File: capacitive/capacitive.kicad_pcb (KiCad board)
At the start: 2 copper layers, 54 parts, among them J102 UART, J103 SWD, J104 TX_PADS, J105 RX_PAD, J106 POWER, Q101 RU1C002ZPTCL, SW101 SW_Push, U101 STM32F070C6T6, U102 TLV9062IDR, U103 SG7050CAN_8.000000M-TJGA3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

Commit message: Generate first revision Gerber files
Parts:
- removed U105: D3V3X4U10LP-7, capacitive:Diode_U-DFN2510-10
- added C107: 100nF 20%, Capacitors_SMD:C_0805_HandSoldering, F.Cu at (113.9, 107.3)
- added D101: ESD9B3.3ST5G, capacitive:SOD-923, F.Cu at (120.3, 75.4)
- added D103: ESD9B3.3ST5G, capacitive:SOD-923, F.Cu at (120.3, 72.5)
- added J101: UL, capacitive:Slide_Drill_Left, F.Cu at (100.0, 95.0)
- added J107: UR, capacitive:Slide_Drill_Right, F.Cu at (100.0, 85.0)
- added J108: LL, capacitive:Slide_Drill_Left, F.Cu at (100.0, 114.0)
- added J109: LR, capacitive:Slide_Drill_Right, F.Cu at (100.0, 115.0)
- added R107: 100k 1%, Resistors_SMD:R_1206_HandSoldering, F.Cu at (113.1, 93.2)
- added R112: 100k 1%, Resistors_SMD:R_1206_HandSoldering, F.Cu at (115.8, 93.1)
- RV102: value 100k linear -> 5k linear; footprint capacitive:Vishay_T73YE -> capacitive:Bourns-PVG5H
- moved TP107 192.4 mm to (87.7, 84.6)
- moved TP109 181.0 mm to (91.3, 67.2)
- moved TP101 150.6 mm to (83.2, 66.4)
- moved TP108 137.2 mm to (125.9, 112.7)
- moved TP102 117.1 mm to (122.2, 112.8), turned to 180 degrees
- moved R101 37.6 mm to (124.4, 106.3), turned to 0 degrees
- moved R105 34.3 mm to (116.0, 109.6), turned to 180 degrees
- moved C118 34.2 mm to (95.6, 58.3)
- moved C110 32.0 mm to (119.4, 106.4), turned to 180 degrees
- moved R106 31.2 mm to (113.9, 105.5), turned to 0 degrees
- moved C113 31.1 mm to (72.3, 88.1), turned to 180 degrees
- moved C103 29.9 mm to (125.2, 100.7), turned to 90 degrees
- moved TP106 28.8 mm to (108.5, 98.8)
- moved R102 28.3 mm to (122.9, 109.6), turned to 180 degrees
- moved U102 27.9 mm to (120.8, 100.7), turned to 180 degrees
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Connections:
- RV101 pad 1: Net-(R101-Pad2) -> Net-(R103-Pad1)
- RV101 pad 3: Net-(R103-Pad1) -> Net-(R101-Pad2)
- RV102 pad 1: GND -> Net-(R107-Pad2)
- RV102 pad 3: +3.3VA -> Net-(R112-Pad1)
- U101 pad 16: /PHASE4 -> /PHASE0
- U101 pad 17: /PHASE5 -> /PHASE2
- U101 pad 18: /PHASE6 -> /PHASE4
- U101 pad 19: /PHASE7 -> /PHASE6
- U101 pad 29: /PHASE0 -> /PHASE1
- U101 pad 30: /PHASE1 -> /PHASE3
- U101 pad 31: /PHASE2 -> /PHASE5
- U101 pad 32: /PHASE3 -> /PHASE7
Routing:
- net GND: track 0.00 -> 440.9 mm, vias 0 -> 27
- net +3V3: track 0.00 -> 145.7 mm, vias 0 -> 2
- net +3.3VA: track 0.00 -> 133.0 mm, vias 0 -> 5
- net /RX_PAD: track 0.00 -> 78.6 mm, vias 0 -> 4
- net +5V: track 0.00 -> 50.1 mm, vias 0 -> 3
- net /PHASE5: track 0.00 -> 45.8 mm, vias 0 -> 6
- net /PHASE0: track 0.00 -> 45.4 mm, vias 0 -> 6
- net /PHASE7: track 0.00 -> 45.0 mm, vias 0 -> 6
- net /PHASE2: track 0.00 -> 44.3 mm, vias 0 -> 6
- net /PHASE4: track 0.00 -> 43.8 mm, vias 0 -> 6
- net /PHASE6: track 0.00 -> 43.8 mm, vias 0 -> 6
- net /PHASE3: track 0.00 -> 43.3 mm, vias 0 -> 6
- net /PHASE1: track 0.00 -> 43.1 mm, vias 0 -> 6
- net /UART_RX: track 0.00 -> 40.7 mm, vias 0 -> 2
- net /UART_TX: track 0.00 -> 38.5 mm, vias 0 -> 2
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- added copper zone on F.Cu, net /RX_PAD
- added copper zone on B.Cu, net GND
- added copper zone on F.Cu, net GND
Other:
- board outline added: 61 x 77 mm

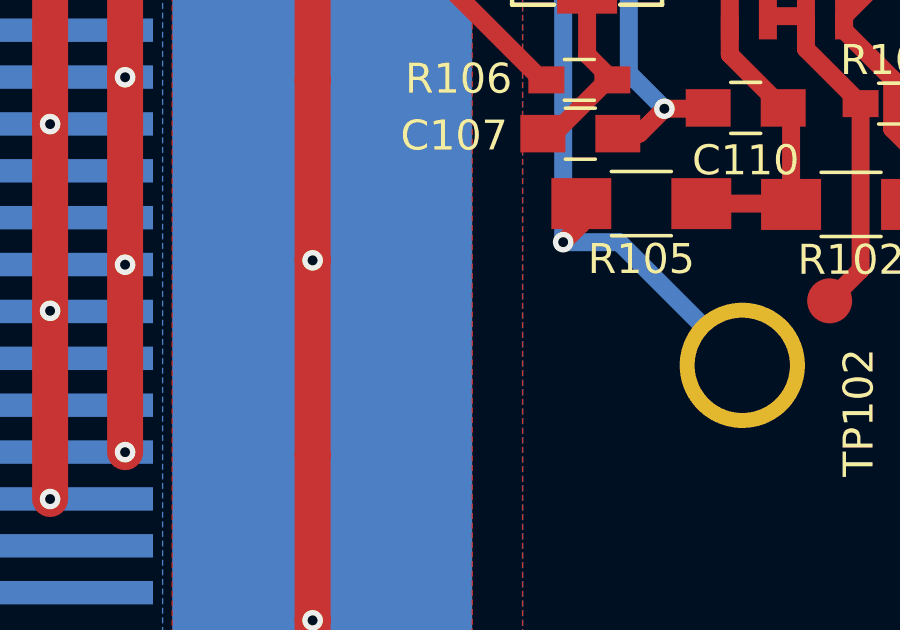
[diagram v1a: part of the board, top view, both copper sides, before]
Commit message: Add input capacitor to help set the input roll-off frequency; it seems to reduce ripple a fair amount
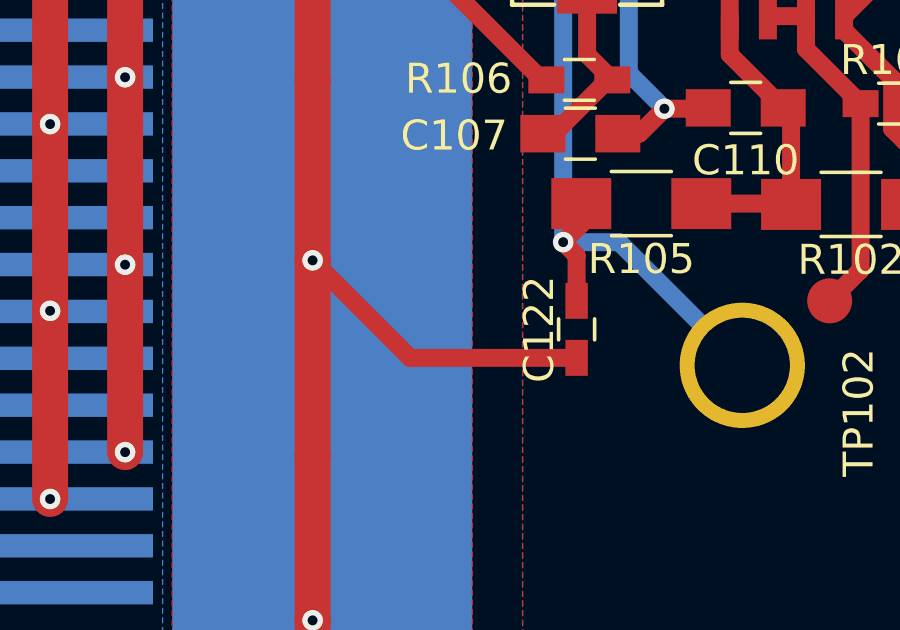
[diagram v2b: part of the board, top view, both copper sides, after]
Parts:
- added C122: 16pF 5%, Capacitors_SMD:C_0603_HandSoldering, F.Cu at (113.8, 113.8)
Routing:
- net /RX_PAD: track 78.6 -> 88.8 mm
- net GND: track 440.9 -> 443.1 mm
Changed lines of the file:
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@@
 (kicad_pcb (version 4) (host pcbnew 4.0.7)
   (general
-    (links 169)
+    (links 171)
     (no_connects 0)
     (area 66.924999 51.924999 128.075001 129.075001)
     (thickness 1.6)
     (drawings 4)
-    (tracks 721)
+    (tracks 725)
     (zones 0)
-    (modules 62)
+    (modules 63)
     (nets 33)
   )
@@
   )
   (setup
-    (last_trace_width 0.3)
+    (last_trace_width 0.6)
     (user_trace_width 0.3)
     (user_trace_width 0.45)
@@
     )
   )
+  (module Capacitors_SMD:C_0603_HandSoldering (layer F.Cu)
+    (at 113.8 113.8 90)
+    (descr "Capacitor SMD 0603, hand soldering")
+    (tags "capacitor 0603")
+    (attr smd)
+    (fp_text reference C122 (at 0 -1.25 90) (layer F.SilkS)
+      (effects (font (size 1 1) (thickness 0.15)))
+    )
+    (fp_text value "16pF 5%" (at 0 1.5 90) (layer F.Fab)
+      (effects (font (size 1 1) (thickness 0.15)))
+    )
+    (fp_text user %R (at 0 -1.25 90) (layer F.Fab)
+      (effects (font (size 1 1) (thickness 0.15)))
+    )
+    (fp_line (start -0.8 0.4) (end -0.8 -0.4) (layer F.Fab) (width 0.1))
+    (fp_line (start 0.8 0.4) (end -0.8 0.4) (layer F.Fab) (width 0.1))
+    (fp_line (start 0.8 -0.4) (end 0.8 0.4) (layer F.Fab) (width 0.1))
+    (fp_line (start -0.8 -0.4) (end 0.8 -0.4) (layer F.Fab) (width 0.1))
+    (fp_line (start -0.35 -0.6) (end 0.35 -0.6) (layer F.SilkS) (width 0.12))
+    (fp_line (start 0.35 0.6) (end -0.35 0.6) (layer F.SilkS) (width 0.12))
+    (fp_line (start -1.8 -0.65) (end 1.8 -0.65) (layer F.CrtYd) (width 0.05))
+    (fp_line (start -1.8 -0.65) (end -1.8 0.65) (layer F.CrtYd) (width 0.05))
+    (fp_line (start 1.8 0.65) (end 1.8 -0.65) (layer F.CrtYd) (width 0.05))
+    (fp_line (start 1.8 0.65) (end -1.8 0.65) (layer F.CrtYd) (width 0.05))
+    (pad 1 smd rect (at -0.95 0 90) (size 1.2 0.75) (layers F.Cu F.Paste F.Mask)
+      (net 23 /RX_PAD))
+    (pad 2 smd rect (at 0.95 0 90) (size 1.2 0.75) (layers F.Cu F.Paste F.Mask)
+      (net 2 GND))
+    (model Capacitors_SMD.3dshapes/C_0603.wrl
+      (at (xyz 0 0 0))
+      (scale (xyz 1 1 1))
+      (rotate (xyz 0 0 0))
+    )
+  )
   (gr_line (start 67 129) (end 67 52) (layer Edge.Cuts) (width 0.15))
   (gr_line (start 128 129) (end 67 129) (layer Edge.Cuts) (width 0.15))
@@
   (segment (start 75.806526 67.71386) (end 76.770596 67.71386) (width 1.2) (layer F.Cu) (net 1))
   (segment (start 76.770596 67.71386) (end 77.75448 67.71386) (width 1.2) (layer F.Cu) (net 1))
+  (segment (start 113.8 112.85) (end 113.8 111.34128) (width 0.6) (layer F.Cu) (net 2))
+  (segment (start 113.8 111.34128) (end 113.35258 110.89386) (width 0.6) (layer F.Cu) (net 2))
   (segment (start 87.03564 77.29728) (end 89.93124 80.19288) (width 0.3) (layer B.Cu) (net 2))
   (segment (start 89.93124 80.19288) (end 91.46794 80.19288) (width 0.3) (layer B.Cu) (net 2))
@@
   (via (at 98.75 111.6457) (size 0.6858) (drill 0.3302) (layers F.Cu B.Cu) (net 22))
   (via (at 98.75 117.8941) (size 0.6858) (drill 0.3302) (layers F.Cu B.Cu) (net 22))
+  (segment (start 113.8 114.75) (end 108.25 114.75) (width 0.6) (layer F.Cu) (net 23))
+  (segment (start 108.25 114.75) (end 105 111.5) (width 0.6) (layer F.Cu) (net 23))
   (segment (start 105 123.5) (end 105 125) (width 1.2) (layer F.Cu) (net 23))
   (segment (start 105 118) (end 105 123.5) (width 1.2) (layer F.Cu) (net 23))

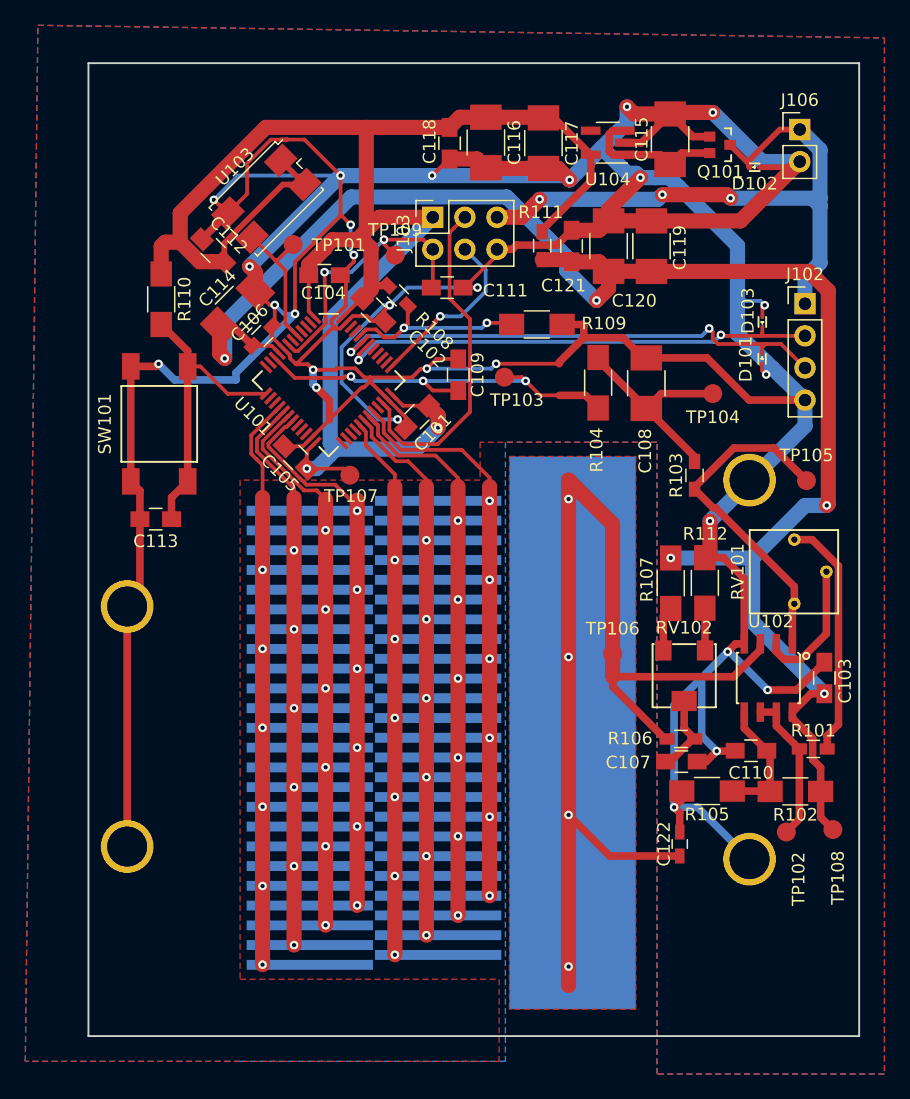
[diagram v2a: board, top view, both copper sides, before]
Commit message: Extend board 2mm to improve mechanical strength of left drill holes and improve ground stitching under MCU
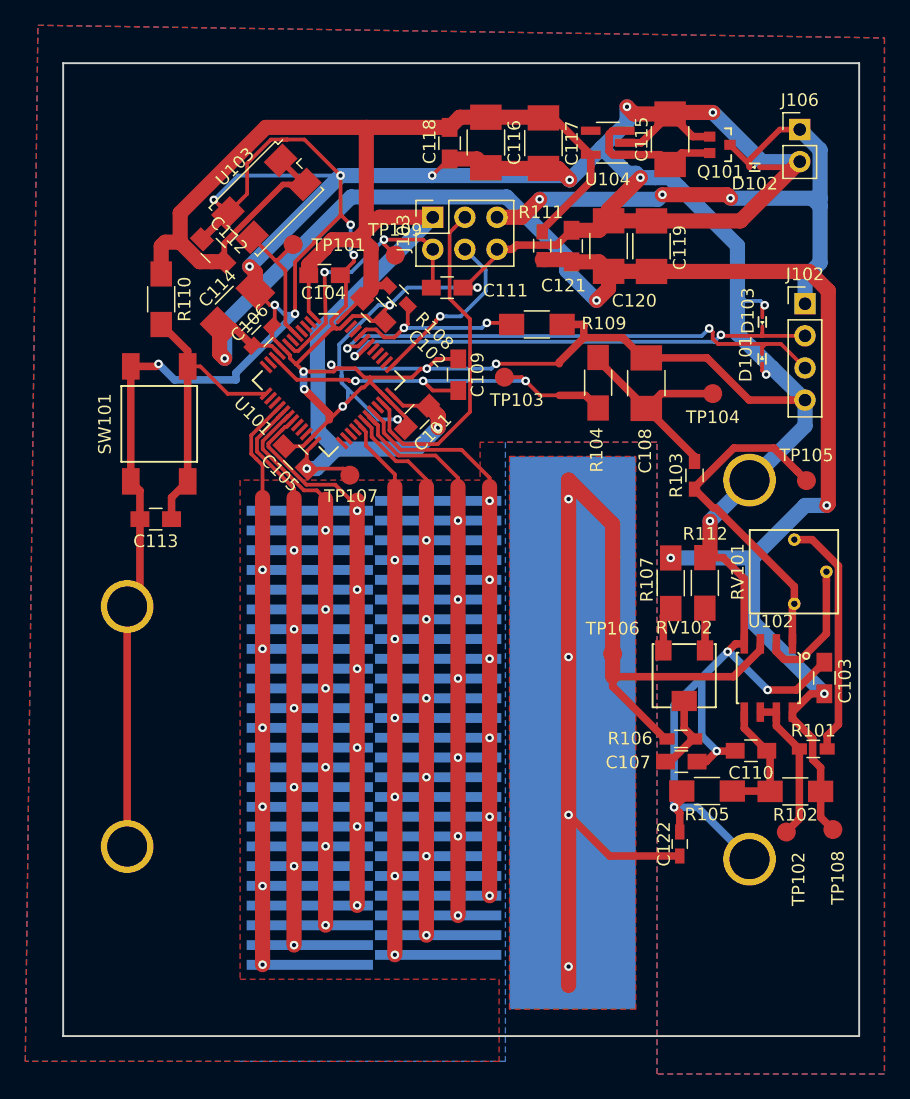
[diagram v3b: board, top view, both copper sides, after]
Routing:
- net GND: track 443.1 -> 455.3 mm, vias 27 -> 29
- net +3V3: track 145.7 -> 146.6 mm
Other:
- board size 61 x 77 mm -> 63 x 77 mm

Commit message: Generate sensor scale
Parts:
- moved J107 30.0 mm to (100.0, 115.0)
- moved J109 30.0 mm to (100.0, 85.0)
- moved J101 20.0 mm to (100.0, 115.0)
- moved J108 19.0 mm to (100.0, 95.0)
- moved TP105 5.41 mm to (120.1, 81.1)
- moved TP102 0.83 mm to (122.4, 112.0)
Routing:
- net Net-(R103-Pad1): track 27.1 -> 22.9 mm
- net /+1V65: track 11.9 -> 11.1 mm
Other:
- board size 63 x 77 mm -> 64 x 77 mm
- board text added: "Rev.1"

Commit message: Change scale size and finish relayout
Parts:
- removed C122: 16pF 5%, Capacitors_SMD:C_0603_HandSoldering
- added C123: 10uF 10%, Capacitors_SMD:C_1210_HandSoldering, F.Cu at (133.8, 82.5)
- added C124: 1.8nF 2%, Capacitors_SMD:C_0603_HandSoldering, F.Cu at (140.4, 94.1)
- added C125: 100nF 2%, Capacitors_SMD:C_1210_HandSoldering, F.Cu at (141.5, 83.4)
- added C126: 33nF 5%, Capacitors_SMD:C_0603_HandSoldering, F.Cu at (133.2, 99.0)
- added C127: 33nF 5%, Capacitors_SMD:C_0603_HandSoldering, F.Cu at (133.2, 100.4)
- added R113: 0, Resistors_SMD:R_0805_HandSoldering, F.Cu at (109.2, 89.7)
- added R114: 0, Resistors_SMD:R_0805_HandSoldering, F.Cu at (114.1, 89.7)
- added R115: DNP, Resistors_SMD:R_0603_HandSoldering, F.Cu at (110.2, 93.2)
- added R117: 100k 1%, Resistors_SMD:R_1206_HandSoldering, F.Cu at (138.2, 93.8)
- added R118: 10k 1%, Resistors_SMD:R_0402, F.Cu at (132.9, 94.2)
- added R119: 1.58k 1%, Resistors_SMD:R_0603_HandSoldering, F.Cu at (136.9, 89.5)
- added R120: 0, Resistors_SMD:R_0805_HandSoldering, F.Cu at (124.5, 76.2)
- added R121: 10k 1%, Resistors_SMD:R_0402, F.Cu at (133.9, 94.2)
- added R122: 100k 1%, Resistors_SMD:R_1206_HandSoldering, F.Cu at (118.9, 97.7)
- added R123: 100k 1%, Resistors_SMD:R_1206_HandSoldering, F.Cu at (118.9, 100.0)
- added R124: DNP, Resistors_SMD:R_0603_HandSoldering, F.Cu at (124.5, 78.3)
- added R125: 0, Resistors_SMD:R_0805_HandSoldering, F.Cu at (121.3, 103.9)
- added R126: 1k 1%, Resistors_SMD:R_0402, F.Cu at (133.3, 97.7)
- added R127: 100k 1%, Resistors_SMD:R_1206_HandSoldering, F.Cu at (135.7, 93.8)
- added TP110: TEST, Measurement_Points:Measurement_Point_Round-SMD-Pad_Small, F.Cu at (133.2, 89.5)
- added TP111: TEST, Measurement_Points:Measurement_Point_Round-SMD-Pad_Small, F.Cu at (116.6, 102.7)
- added TP112: TEST, Measurement_Points:Measurement_Point_Round-SMD-Pad_Small, F.Cu at (140.0, 98.2)
- C109: value 10nF 1% -> 10 nF 1%
- D101, D103: moved to B.Cu
- J103: footprint Socket_Strips:Socket_Strip_Straight_2x03_Pitch2.54mm -> Socket_Strips:Socket_Strip_Straight_2x03_Pitch2.54mm_SMD
- J106: footprint Socket_Strips:Socket_Strip_Straight_1x02_Pitch2.54mm -> capacitive:Power_Pads
- R101: value 100 1% -> 1k
- R102, R105: value 100k 1% -> 1k 1%; footprint Resistors_SMD:R_1206_HandSoldering -> Resistors_SMD:R_0402
- R104: footprint Resistors_SMD:R_1206_HandSoldering -> Resistors_SMD:R_0805_HandSoldering
- R106: value 10M 5% -> 100k 1%; footprint Resistors_SMD:R_0603_HandSoldering -> Resistors_SMD:R_1206_HandSoldering
- U102: value TLV9062IDR -> TLV9064IPWR; footprint capacitive:TI_SOIC-8 -> capacitive:TI_TSSOP14
- moved TP108 44.8 mm to (132.9, 68.4)
- moved C109 44.6 mm to (127.7, 108.4), turned to 0 degrees
- moved TP103 39.0 mm to (123.9, 107.7)
- moved TP104 35.6 mm to (127.6, 112.0)
- moved R104 35.4 mm to (127.7, 106.3), turned to 180 degrees
- moved C118 35.0 mm to (130.4, 62.2), turned to 90 degrees
- moved J101 35.0 mm to (100.0, 80.0)
- moved C121 35.0 mm to (138.4, 77.5), turned to 0 degrees
- moved TP107 33.5 mm to (118.2, 70.8)
- moved R111 32.0 mm to (134.9, 65.5), turned to 0 degrees
- moved C108 31.0 mm to (127.6, 103.6), turned to 0 degrees
- moved C120 30.3 mm to (138.3, 70.2), turned to 0 degrees
- moved C119 27.7 mm to (138.3, 73.7), turned to 0 degrees
- moved TP102 27.6 mm to (133.9, 87.0), turned to 0 degrees
- moved R105 27.1 mm to (131.2, 87.3), turned to 270 degrees
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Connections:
- C109 pad 1: /ADC_IN -> /A
- C110 pad 1: Net-(C110-Pad1) -> /+1V65
- Q101 pad 2: Net-(C115-Pad1) -> +5V
- Q101 pad 3: +5V -> Net-(C115-Pad1)
- R102 pad 2: Net-(C110-Pad1) -> /+1V65
- R104 pad 2: /ADC_IN -> /A
- R105 pad 1: Net-(C110-Pad1) -> /+1V65
- R106 pad 1: /RX_PAD -> Net-(R106-Pad1)
- TP103 pad 1: /ADC_IN -> /A
- TP106 pad 1: /RX_PAD -> Net-(R106-Pad1)
- U102 pad 3: /RX_PAD -> Net-(R106-Pad1)
- U102 pad 4: GND -> +3.3VA
- U102 pad 5: Net-(C110-Pad1) -> Net-(R125-Pad2)
- U102 pad 6: /+1V65 -> Net-(R122-Pad2)
- U102 pad 7: /+1V65 -> Net-(R118-Pad1)
- U102 pad 8: +3.3VA -> Net-(C127-Pad1)
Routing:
- net /RX_PAD: track 88.8 -> 39.1 mm, vias 4 -> 5
- net /A: track 0.00 -> 41.7 mm, vias 0 -> 2
- net /+1V65: track 11.1 -> 47.2 mm, vias 0 -> 5
- net Net-(R118-Pad1): track 0.00 -> 35.9 mm, vias 0 -> 2
- net GND: track 455.3 -> 426.2 mm, vias 29 -> 23
- net Net-(C125-Pad1): track 0.00 -> 24.8 mm
- net Net-(C107-Pad1): track 6.41 -> 26.8 mm
- net Net-(C124-Pad2): track 0.00 -> 18.3 mm, vias 0 -> 3
- net +3.3VA: track 133.0 -> 116.1 mm, vias 5 -> 3
- net Net-(R101-Pad2): track 19.2 -> 2.63 mm
- net Net-(R126-Pad1): track 0.00 -> 14.8 mm
- net Net-(R106-Pad1): track 0.00 -> 14.1 mm
- net /ZERO: track 23.9 -> 37.4 mm
- net Net-(R125-Pad2): track 0.00 -> 13.2 mm
- net Net-(C124-Pad1): track 0.00 -> 13.0 mm
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- removed copper zone on F.Cu, net /RX_PAD
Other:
- board size 64 x 77 mm -> 78 x 72 mm
- board text added: "Rev.2"
- board text removed: "Rev.1"
